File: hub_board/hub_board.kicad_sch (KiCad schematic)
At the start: 13 parts, among them J1 Fingers, J2 Fingers, J3 Fingers, J4 Fingers, J5 1473149-4, U1 AP2112K-3.3TRG1

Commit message: Finish hub board layout
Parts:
- C4: symbol Device:C_Small_US -> Device:C
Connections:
- net GND: now also J5.SH1 (SHIELD), J5.SH2 (SHIELD__1), RJ1.15, RJ1.16, USB1.7, USB1.8
- net LED1: now also J5.111; no longer J5.85
- net LED2: now also J5.109; no longer J5.87
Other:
- moved on the sheet: C4

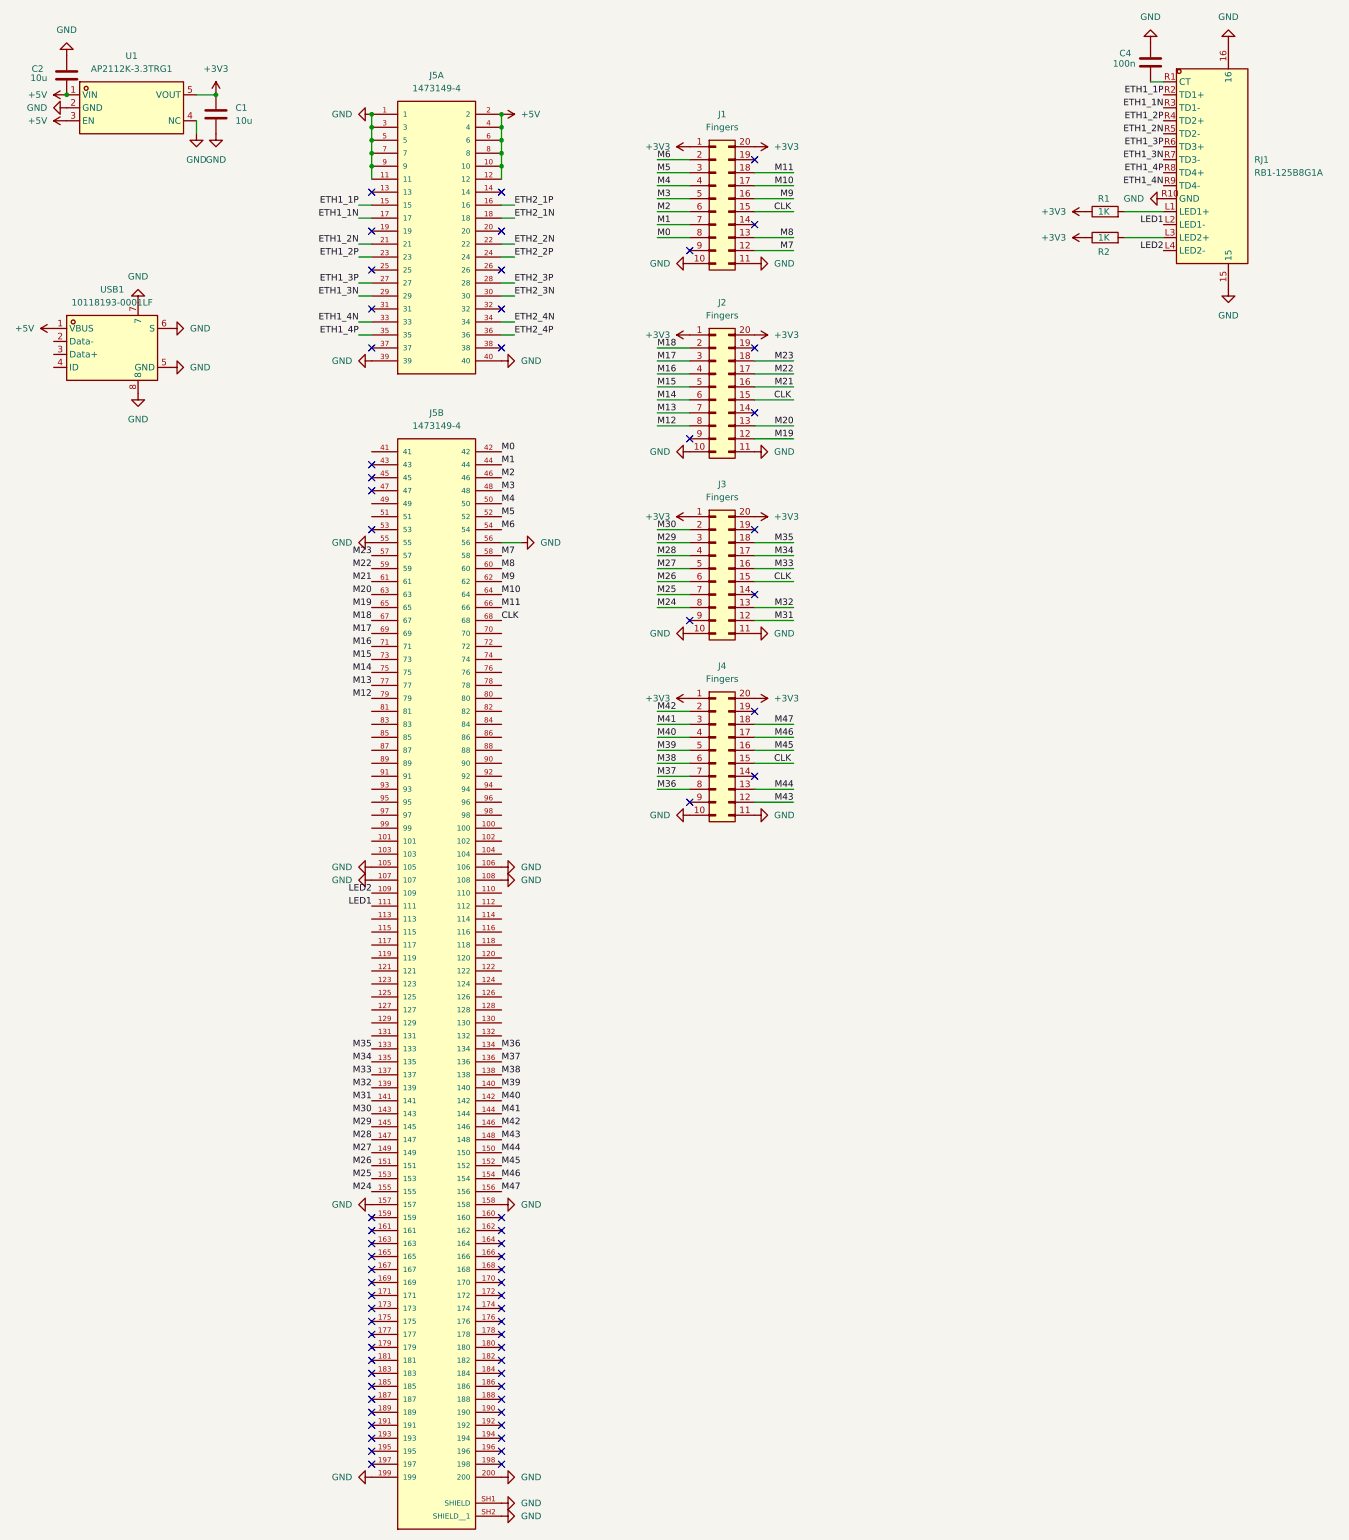
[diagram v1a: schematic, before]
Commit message: Fix DDR2 connector position & reroute; add test points
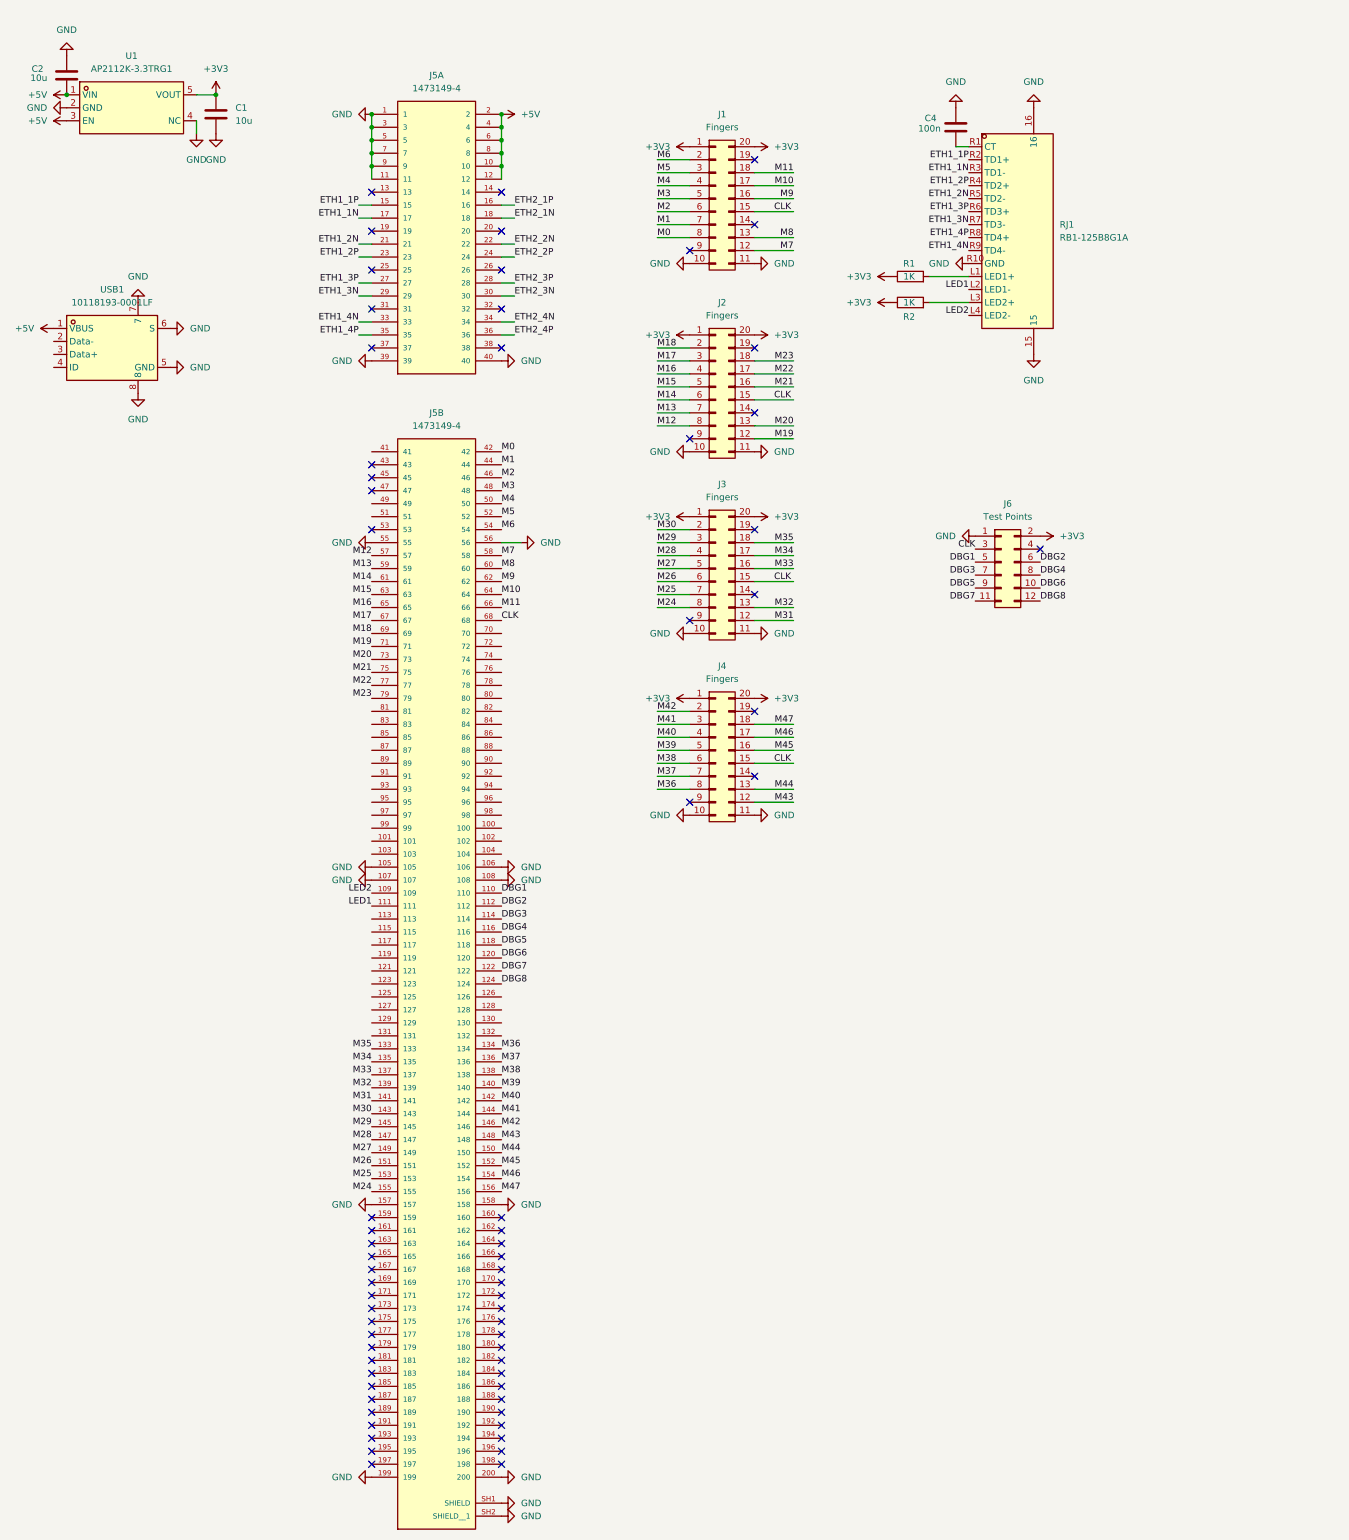
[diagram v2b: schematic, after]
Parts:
- added J6: Test Points, symbol Connector_Generic:Conn_02x06_Odd_Even
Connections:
- net +3V3: now also J6.2 (Pin_2)
- net CLK: now also J6.3 (Pin_3)
- net GND: now also J6.1 (Pin_1)
- net M12: now also J5.57; no longer J5.79
- net M13: now also J5.59; no longer J5.77
- net M14: now also J5.61; no longer J5.75
- net M15: now also J5.63; no longer J5.73
- net M16: now also J5.65; no longer J5.71
- net M17: now also J5.67; no longer J5.69
- net M18: now also J5.69; no longer J5.67
- net M19: now also J5.71; no longer J5.65
- net M20: now also J5.73; no longer J5.63
- net M21: now also J5.75; no longer J5.61
- net M22: now also J5.77; no longer J5.59
- net M23: now also J5.79; no longer J5.57
- net DBG1: now reaches J5.110
- net DBG1: now also J6.5 (Pin_5)
- net DBG2: now reaches J5.112
- net DBG2: now also J6.6 (Pin_6)
- net DBG3: now reaches J5.114
- net DBG3: now also J6.7 (Pin_7)
- net DBG4: now reaches J5.116
- net DBG4: now also J6.8 (Pin_8)
- net DBG5: now reaches J5.118
- net DBG5: now also J6.9 (Pin_9)
- net DBG6: now reaches J5.120
- net DBG6: now also J6.10 (Pin_10)
- net DBG7: now reaches J5.122
- net DBG7: now also J6.11 (Pin_11)
- net DBG8: now reaches J5.124
- net DBG8: now also J6.12 (Pin_12)
- no-connect marks 66 -> 67
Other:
- moved on the sheet: C4, R1, R2, RJ1

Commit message: Redo layout (wip)
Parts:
- removed USB1: 10118193-0001LF, hub:MICRO-USB-SMD_10118193-0001LF, symbol Hub:10118193-0001LF
- added C3: 10u, symbol Device:C
- added J7: 54-00166, 54-00166:TENSILITY_54-00166, symbol 54-00166:54-00166
- R1, R2: value 1K -> 220
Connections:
- net +5V: now also C3.1, J7.A
- net DBG1: now also J5.123; no longer J5.110
- net DBG2: now also J5.121; no longer J5.112
- net DBG3: now also J5.119; no longer J5.114
- net DBG4: now also J5.117; no longer J5.116
- net DBG5: now also J5.115; no longer J5.118
- net DBG6: now also J5.113; no longer J5.120
- net DBG7: now also J5.111; no longer J5.122
- net DBG8: now also J5.109; no longer J5.124
- net ETH1_1N: no longer RJ1.R3 (TD1-)
- net ETH1_1P: no longer RJ1.R2 (TD1+)
- net ETH1_2N: no longer RJ1.R5 (TD2-)
- net ETH1_2P: no longer RJ1.R4 (TD2+)
- net ETH1_3N: no longer RJ1.R7 (TD3-)
- net ETH1_3P: no longer RJ1.R6 (TD3+)
- net ETH1_4N: no longer RJ1.R9 (TD4-)
- net ETH1_4P: no longer RJ1.R8 (TD4+)
- net ETH2_1N: now also RJ1.R3 (TD1-)
- net ETH2_1P: now also RJ1.R2 (TD1+)
- net ETH2_2N: now also J5.24, RJ1.R5 (TD2-); no longer J5.22
- net ETH2_2P: now also J5.22, RJ1.R4 (TD2+); no longer J5.24
- net ETH2_3N: now also RJ1.R7 (TD3-)
- net ETH2_3P: now also RJ1.R6 (TD3+)
- net ETH2_4N: now also J5.36, RJ1.R9 (TD4-); no longer J5.34
- net ETH2_4P: now also J5.34, RJ1.R8 (TD4+); no longer J5.36
- net GND: now also C3.2, J7.B, J7.C
- net LED1: now also J5.112; no longer J5.111
- net LED2: now also J5.110; no longer J5.109
- net M0: now also J5.156; no longer J5.42
- net M1: now also J5.154; no longer J5.44
- net M10: now also J5.136; no longer J5.64
- net M11: now also J5.134; no longer J5.66
- net M12: now also J5.133; no longer J5.57
- net M13: now also J5.135; no longer J5.59
- net M14: now also J5.137; no longer J5.61
- net M15: now also J5.139; no longer J5.63
- net M16: now also J5.141; no longer J5.65
- net M17: now also J5.143; no longer J5.67
- net M18: now also J5.145; no longer J5.69
- net M19: now also J5.147; no longer J5.71
- net M2: now also J5.152; no longer J5.46
- net M20: now also J5.149; no longer J5.73
- net M21: now also J5.151; no longer J5.75
- net M22: now also J5.153; no longer J5.77
- net M23: now also J5.155; no longer J5.79
- net M24: now also J5.57; no longer J5.155
- net M25: now also J5.59; no longer J5.153
- net M26: now also J5.61; no longer J5.151
- net M27: now also J5.63; no longer J5.149
- net M28: now also J5.65; no longer J5.147
- net M29: now also J5.67; no longer J5.145
- net M3: now also J5.150; no longer J5.48
- net M30: now also J5.69; no longer J5.143
- net M31: now also J5.71; no longer J5.141
- net M32: now also J5.73; no longer J5.139
- net M33: now also J5.75; no longer J5.137
- net M34: now also J5.77; no longer J5.135
- net M35: now also J5.79; no longer J5.133
- net M36: now also J5.66; no longer J5.134
- net M37: now also J5.64; no longer J5.136
- net M38: now also J5.62; no longer J5.138
- net M39: now also J5.60; no longer J5.140
- net M4: now also J5.148; no longer J5.50
- net M40: now also J5.58; no longer J5.142
- net M41: now also J5.54; no longer J5.144
- net M42: now also J5.52; no longer J5.146
- net M43: now also J5.50; no longer J5.148
- net M44: now also J5.48; no longer J5.150
- net M45: now also J5.46; no longer J5.152
- net M46: now also J5.44; no longer J5.154
- net M47: now also J5.42; no longer J5.156
- net M5: now also J5.146; no longer J5.52
- net M6: now also J5.144; no longer J5.54
- net M7: now also J5.142; no longer J5.58
- net M8: now also J5.140; no longer J5.60
- net M9: now also J5.138; no longer J5.62

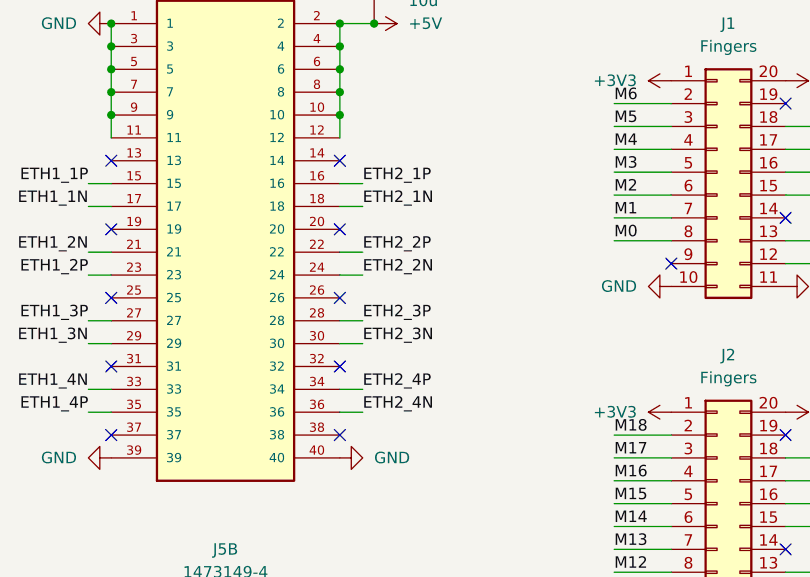
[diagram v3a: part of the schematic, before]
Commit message: Flip ethernet port & fix routing
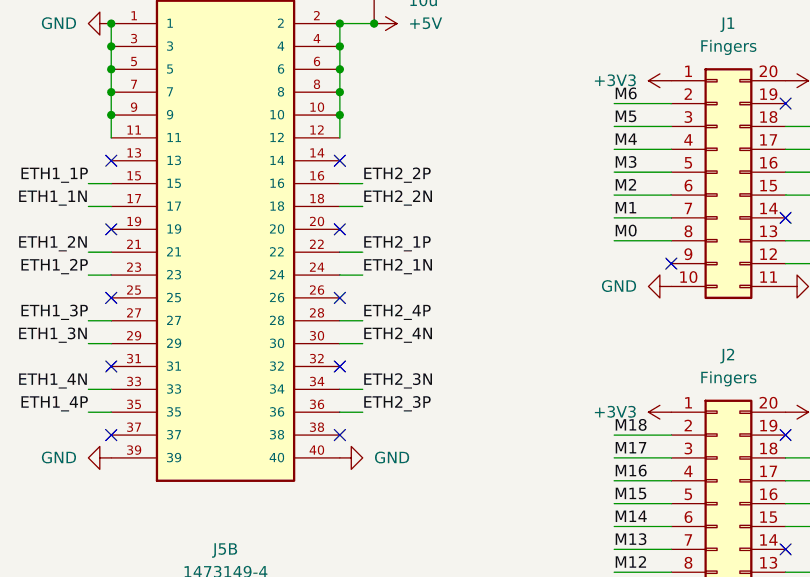
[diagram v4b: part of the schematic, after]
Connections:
- net ETH2_1N: now also J5.24; no longer J5.18
- net ETH2_1P: now also J5.22; no longer J5.16
- net ETH2_2N: now also J5.18; no longer J5.24
- net ETH2_2P: now also J5.16; no longer J5.22
- net ETH2_3N: now also J5.34; no longer J5.30
- net ETH2_3P: now also J5.36; no longer J5.28
- net ETH2_4N: now also J5.30; no longer J5.36
- net ETH2_4P: now also J5.28; no longer J5.34
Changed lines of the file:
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@@
 		)
 	)
-	(label "ETH2_2N"
+	(label "ETH2_1N"
 		(at 114.3 63.5 0)
 		(effects
@@
 		)
 	)
-	(label "ETH2_1P"
+	(label "ETH2_2P"
 		(at 114.3 53.34 0)
 		(effects
@@
 		)
 	)
-	(label "ETH2_3P"
+	(label "ETH2_4P"
 		(at 114.3 68.58 0)
 		(effects
@@
 		)
 	)
-	(label "ETH2_4P"
+	(label "ETH2_3N"
 		(at 114.3 76.2 0)
 		(effects
@@
 		)
 	)
-	(label "ETH2_4N"
+	(label "ETH2_3P"
 		(at 114.3 78.74 0)
 		(effects
@@
 		)
 	)
-	(label "ETH2_3N"
+	(label "ETH2_4N"
 		(at 114.3 71.12 0)
 		(effects
@@
 		)
 	)
-	(label "ETH2_1N"
+	(label "ETH2_2N"
 		(at 114.3 55.88 0)
 		(effects
@@
 		)
 	)
-	(label "ETH2_2P"
+	(label "ETH2_1P"
 		(at 114.3 60.96 0)
 		(effects
